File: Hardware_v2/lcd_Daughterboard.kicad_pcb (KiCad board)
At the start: 2 copper layers, 68 x 45 mm, 5 parts, among them J3 Conn_01x03_Pin, J4 Conn_01x03_Pin, J5 Conn_01x02_Pin, J6 Conn_01x02_Pin, U1 ILI9341_SPI_Bare

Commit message: Routing of component board
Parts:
- J3, J4, J5, J6: moved to B.Cu
- moved J3 63.9 mm to (166.0, 108.5), turned to 180 degrees
- moved J6 63.9 mm to (102.1, 133.9), turned to 180 degrees
- moved J5 25.4 mm to (102.1, 108.5), turned to 180 degrees
- moved J4 22.9 mm to (166.0, 131.4), turned to 180 degrees
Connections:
- J3 pad 1: /LCD_RESET -> /LCD_DC
- J3 pad 3: /LCD_DC -> /LCD_RESET
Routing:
- net /LCD_DC: track 21.2 -> 60.2 mm
- net /LCD_RESET: track 22.6 -> 47.5 mm
- net +3.3V: track 50.5 -> 41.1 mm
- net GND: track 9.60 -> 2.54 mm
- net /LCD_MOSI: track 47.0 -> 51.5 mm
- net /LCD_SCK: track 48.1 -> 50.4 mm
- net /BackLight: track 25.1 -> 24.2 mm

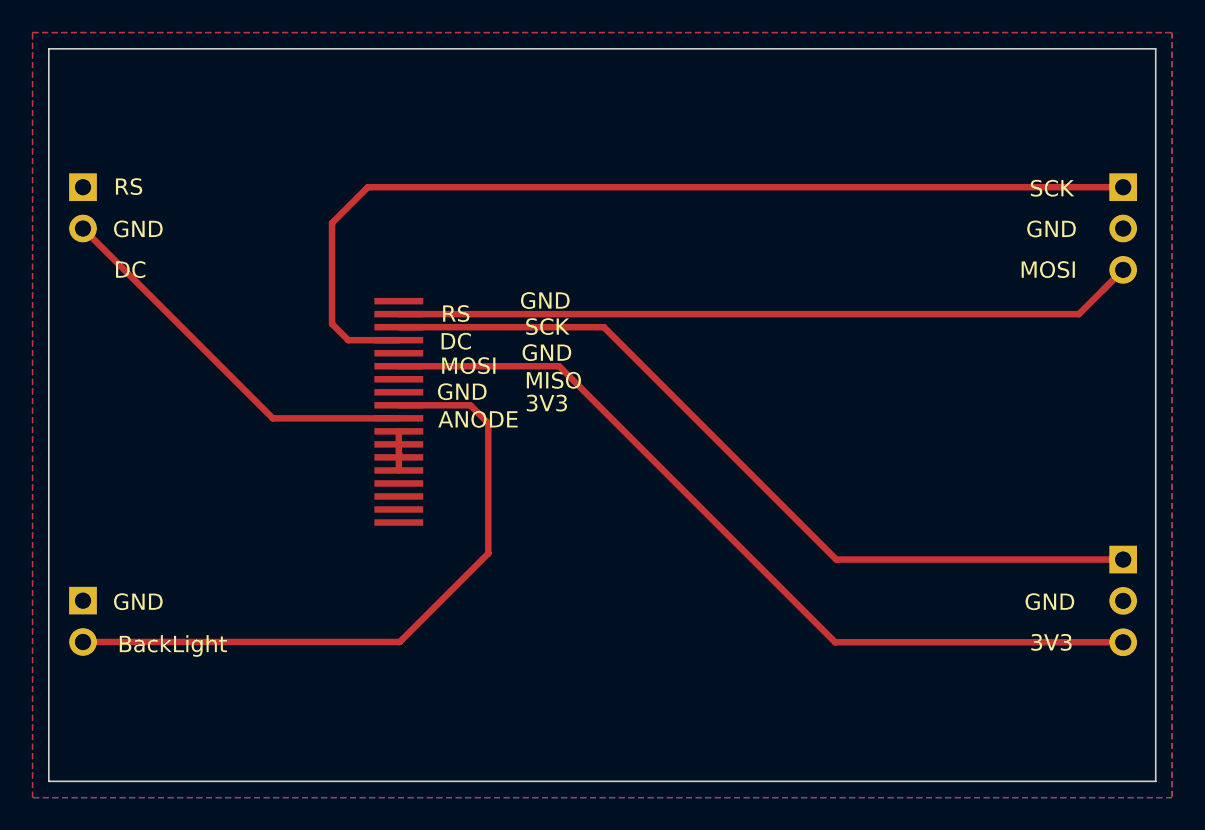
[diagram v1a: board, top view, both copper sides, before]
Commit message: Folder reorganisation
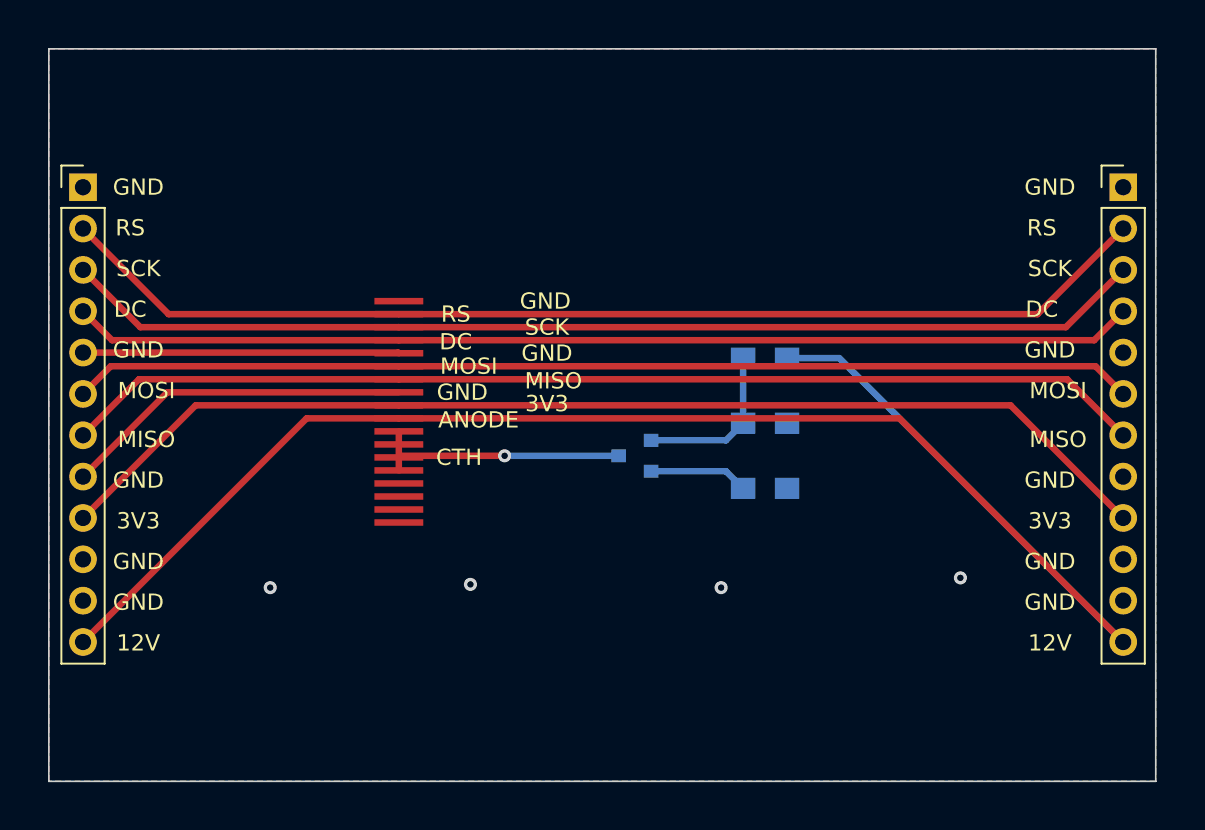
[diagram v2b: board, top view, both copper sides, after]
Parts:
- removed J3, J4: Conn_01x03_Pin, Connector_PinHeader_2.54mm:PinHeader_1x03_P2.54mm_Vertical
- removed J5, J6: Conn_01x02_Pin, Connector_PinHeader_2.54mm:PinHeader_1x02_P2.54mm_Vertical
- added J1: Conn_01x12, Pin_Headers:Pin_Header_Straight_1x12_Pitch2.54mm, F.Cu at (102.1, 108.5)
- added J2: Conn_01x12, Pin_Headers:Pin_Header_Straight_1x12_Pitch2.54mm, F.Cu at (166.0, 108.5)
- added Q1: MMBT3904, TO_SOT_Packages_SMD:SOT-23, B.Cu at (136.0, 125.0)
- added R1: 220, Resistors_SMD:R_0805_HandSoldering, B.Cu at (144.0, 119.0)
- added R2: 1k, Resistors_SMD:R_0805_HandSoldering, B.Cu at (144.0, 123.0)
- added R3: 100, Resistors_SMD:R_0805_HandSoldering, B.Cu at (144.0, 127.0)
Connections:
- U1 pad 10: /BackLight -> VCC
- U1 pad 11: GND -> LCD_CATHODE
- U1 pad 12: GND -> LCD_CATHODE
- U1 pad 13: GND -> LCD_CATHODE
- U1 pad 14: GND -> LCD_CATHODE
- U1 pad 15: unconnected-(U1-XL-Pad15) -> Net-(U1-Pad15)
- U1 pad 16: unconnected-(U1-YU-Pad16) -> Net-(U1-Pad16)
- U1 pad 17: unconnected-(U1-XR-Pad17) -> Net-(U1-Pad17)
- U1 pad 18: unconnected-(U1-YD-Pad18) -> Net-(U1-Pad18)
- U1 pad 2: /LCD_RESET -> LCD_RESET
- U1 pad 3: /LCD_SCK -> LCD_SCK
- U1 pad 4: /LCD_DC -> LCD_DC
- U1 pad 6: /LCD_MOSI -> LCD_MOSI
- U1 pad 7: unconnected-(U1-MISO-Pad7) -> LCD_MISO
- U1 pad 9: +3.3V -> +3V3
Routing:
- net VCC: track 0.00 -> 103.2 mm
- net +3V3: track 0.00 -> 69.6 mm
- net LCD_RESET: track 0.00 -> 68.3 mm
- net LCD_SCK: track 0.00 -> 66.8 mm
- net LCD_MISO: track 0.00 -> 66.7 mm
- net LCD_DC: track 0.00 -> 65.4 mm
- net LCD_MOSI: track 0.00 -> 65.3 mm
- net /LCD_DC: track 60.2 -> 0.00 mm
- net /LCD_MOSI: track 51.5 -> 0.00 mm
- net /LCD_SCK: track 50.4 -> 0.00 mm
- net /LCD_RESET: track 47.5 -> 0.00 mm
- net +3.3V: track 41.1 -> 0.00 mm
- net GND: track 2.54 -> 41.0 mm, vias 0 -> 4
- net /BackLight: track 24.2 -> 0.00 mm
- net LCD_CATHODE: track 0.00 -> 15.9 mm, vias 0 -> 1
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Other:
- net class Default added: clearance 0.2, trace_width 0.4, via_dia 0.8, via_drill 0.4
- board text added: "12V"
- board text added: "CTH"
- board text added: "LCD Daughterboard v1"
- board text removed: "BackLight"
- board text removed: "LCD Daughterboard v2"
